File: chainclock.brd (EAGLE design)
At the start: 60 x 40 mm, 11 parts

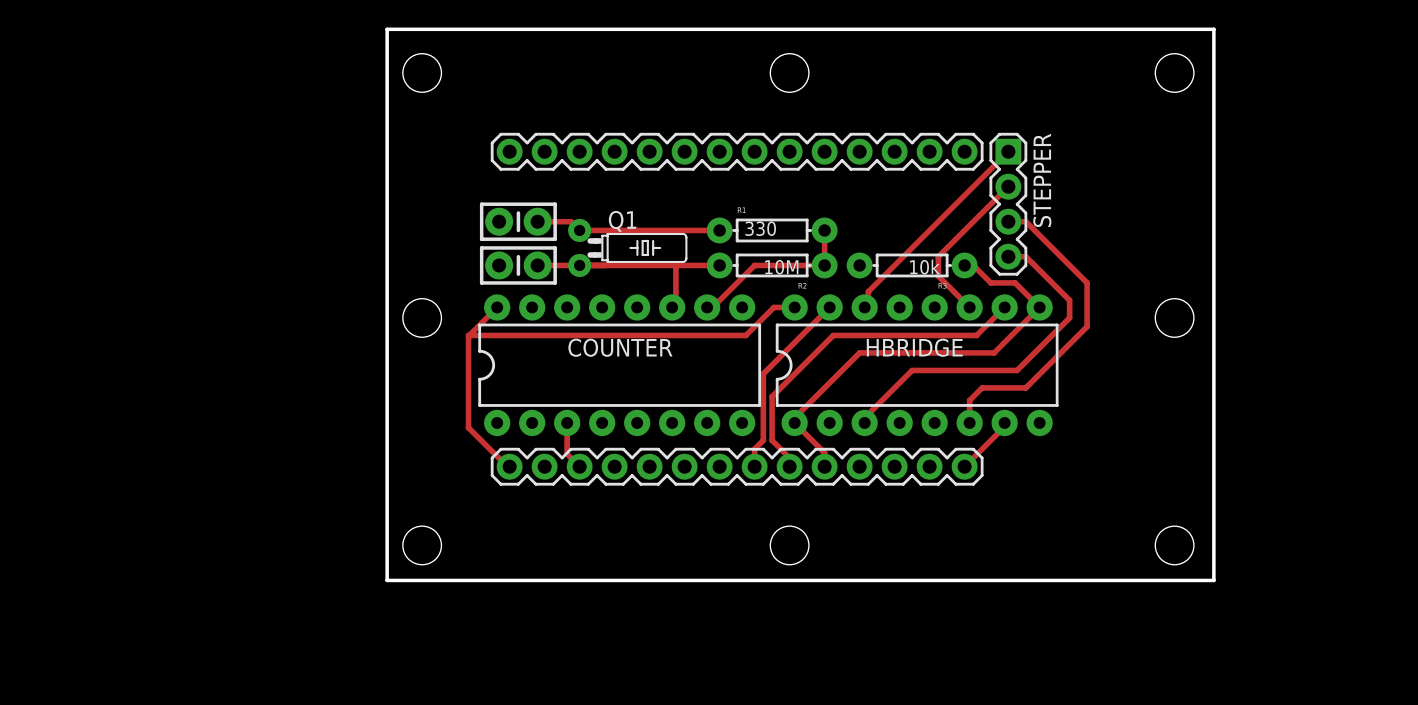
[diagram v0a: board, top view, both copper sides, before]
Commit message: Updates to chainclock, adding motor
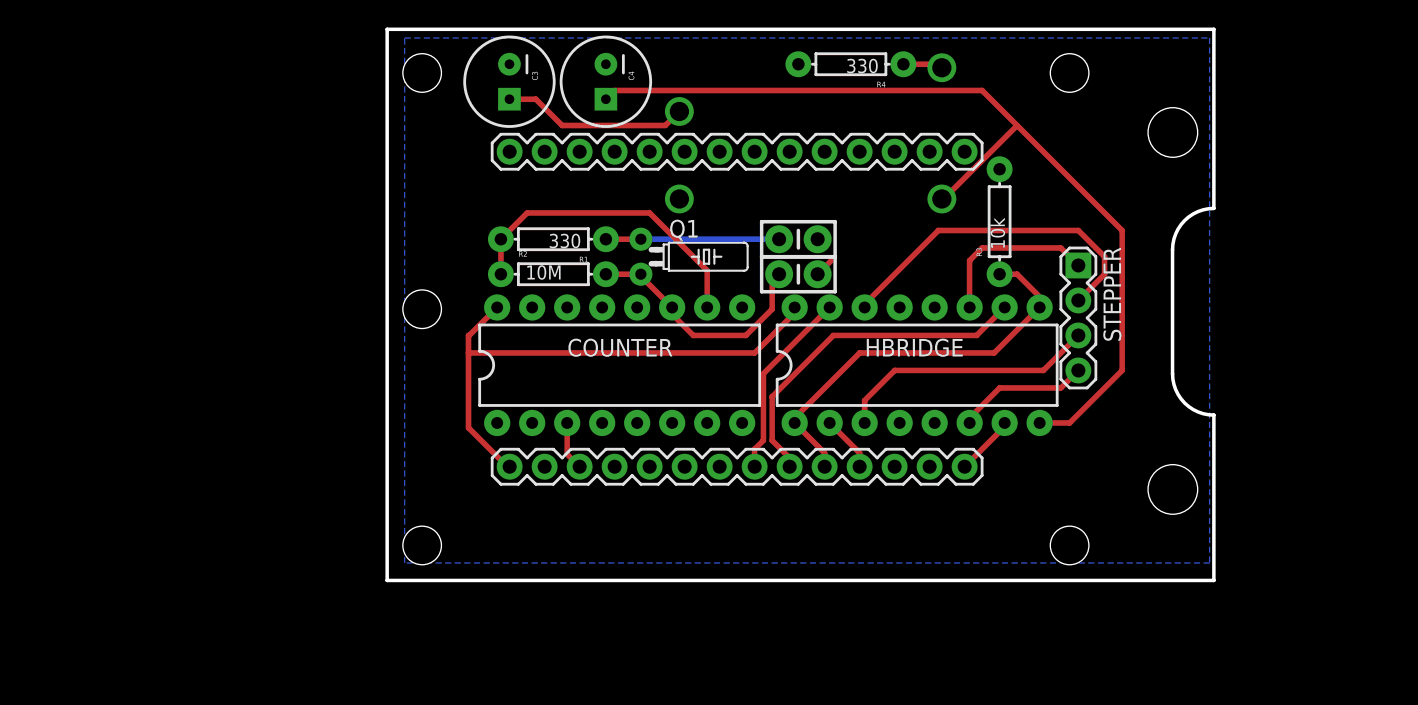
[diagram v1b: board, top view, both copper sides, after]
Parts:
- added C3, C4: (no value), SparkFun-Passives:CPOL-RADIAL-100UF-25V
- added R4: 330, SparkFun-Resistors:AXIAL-0.3EZ
- added U$1: PTN0405C, desjardins:EUU4
- added U$2: (no value), desjardins:NEMA14
- moved C2 20.4 mm to (29.8, 24.8), turned to 0 degrees
- moved C1 20.3 mm to (29.8, 22.2), turned to 0 degrees
- moved R1 15.9 mm to (12.1, 24.8), turned to 180 degrees
- moved R2 15.9 mm to (12.1, 22.2), turned to 0 degrees
- moved STEPPER 9.69 mm to (50.2, 22.9)
- moved R3 7.10 mm to (44.5, 26.0), turned to 90 degrees
- moved Q1 4.49 mm to (18.4, 23.5)
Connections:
- new net N$3: R4.P$1, U$1.3
- new net VDD12: C4.1, HBRIDGE.8, U$1.4
- new net VIN: C3.1, U$1.2
- net 1A: now also ARDUNOFIO.11
- net 1Y: now also STEPPER.3; no longer STEPPER.4
- net 2Y: now also STEPPER.4; no longer STEPPER.3
- net 3Y: now also STEPPER.1; no longer STEPPER.2
- net 4Y: now also STEPPER.2; no longer STEPPER.1
- net GND: now also C3.2, C4.2, R4.P$2, U$1.1
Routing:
- net VDD12: track 0.00 -> 67.3 mm
- net VIN: track 0.00 -> 13.5 mm
- net 2Y: track 23.1 -> 9.68 mm
- net RTC: track 12.3 -> 22.7 mm
- net 4Y: track 15.6 -> 24.6 mm
- net 1Y: track 25.3 -> 19.1 mm
- net 1A: track 0.00 -> 4.08 mm
- net N$3: track 0.00 -> 2.90 mm
- net EN: track 32.2 -> 30.1 mm
- net GND: track 0.00 -> 1.36 mm
- net N$1: track 13.5 -> 12.6 mm
- net 3V32: track 38.2 -> 39.0 mm
- added copper zone on layer 16, net GND
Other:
- outline, holes or cut-outs redrawn

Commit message: Move some stuff around
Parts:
- removed FRAME1: FRAME-LETTER, SparkFun-Aesthetics:CREATIVE_COMMONS
- R4: value 330 -> 1.35k
- moved C4 24.8 mm to (40.6, 36.2)
- moved STEPPER 10.3 mm to (42.5, 29.8)
- moved R4 5.08 mm to (28.6, 37.5)
- moved U$1 5.08 mm to (14.6, 38.7)
- moved ARDUNOFIO 4.45 mm to (38.7, 6.99)
- moved C1 4.45 mm to (25.4, 22.2)
- moved C2 4.45 mm to (25.4, 24.8)
- moved COUNTER 4.45 mm to (12.4, 15.6)
- moved HBRIDGE 4.45 mm to (34.0, 15.6)
- moved R3 4.45 mm to (40.0, 26.0)
- moved R1 4.44 mm to (7.62, 24.8)
- moved R2 4.44 mm to (7.62, 22.2)
- moved Q1 4.44 mm to (14.0, 23.5)
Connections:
- net 1Y: now also STEPPER.4; no longer STEPPER.3
- net 2Y: now also STEPPER.3; no longer STEPPER.4
- net 3Y: now also STEPPER.2; no longer STEPPER.1
- net 4Y: now also STEPPER.1; no longer STEPPER.2
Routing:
- net VDD12: track 67.3 -> 36.7 mm
- net 2Y: track 9.68 -> 18.1 mm
- net 4Y: track 24.6 -> 16.6 mm
- net VIN: track 13.5 -> 7.62 mm
- net 1Y: track 19.1 -> 22.3 mm
- net 3Y: track 12.2 -> 9.45 mm
- net EN: track 30.1 -> 29.6 mm

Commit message: Add logo
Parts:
- added U$3: (no value), desjardins:LOGO
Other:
- board text added: "cjd@chrisd.info http://blog.chrisd.info v1.0 (c) 2014"
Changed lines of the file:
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@@
 <wire x1="57" y1="24" x2="60" y2="27" width="0.254" layer="20" curve="-90"/>
 <wire x1="60" y1="27" x2="60" y2="40" width="0.254" layer="20"/>
+<text x="29.845" y="2.54" size="1.016" layer="21">cjd@chrisd.info
+http://blog.chrisd.info
+v1.0 (c) 2014</text>
 </plain>
 <attributes>
@@
 <element name="R4" library="SparkFun-Resistors" package="AXIAL-0.3EZ" value="1.35k" x="28.575" y="37.465" rot="R180"/>
 <element name="U$2" library="desjardins" package="NEMA14" value="" x="87.63" y="1.905" rot="R90"/>
+<element name="U$3" library="desjardins" package="LOGO" value="" x="5.08" y="1.905"/>
 </elements>
 <signals>
@@
 </board>
 </drawing>
+<compatibility>
+<note version="6.3" minversion="6.2.2" severity="warning">
+Since Version 6.2.2 text objects can contain more than one line,
+which will not be processed correctly with this version.
+</note>
+</compatibility>
 </eagle>

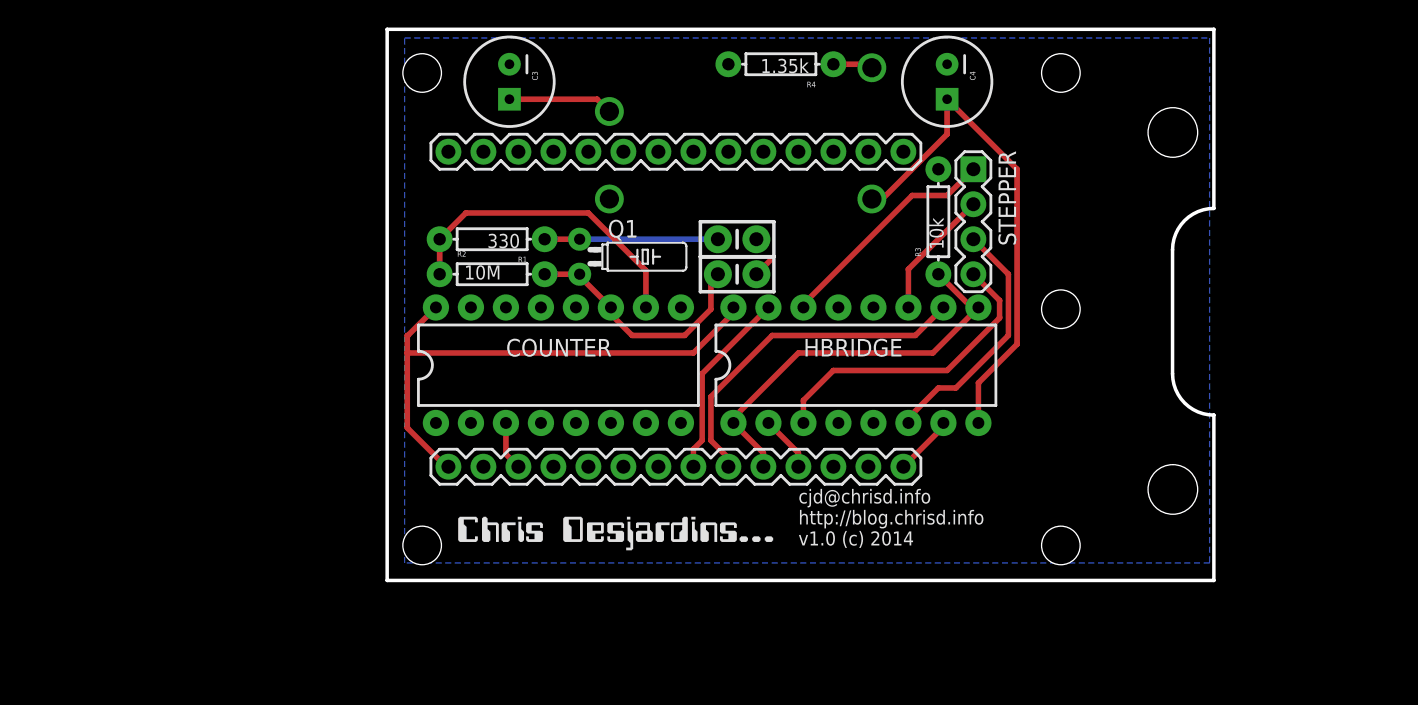
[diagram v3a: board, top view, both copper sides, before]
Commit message: Move around voltage reg
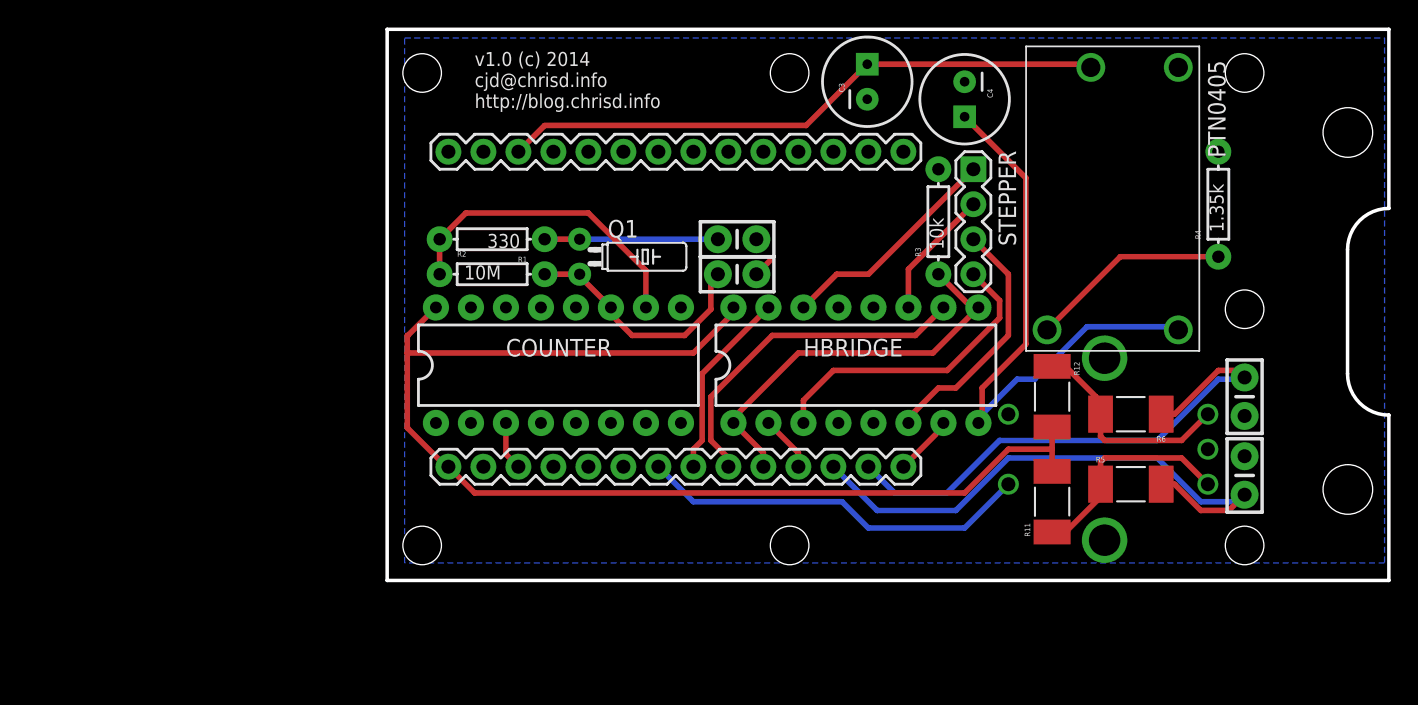
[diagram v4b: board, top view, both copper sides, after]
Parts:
- removed U$1: PTN0405C, desjardins:EUU4
- added C5, C6: .01uf, SparkFun-Capacitors:CAP-PTH-SMALL-KIT
- added PTN0405: PTN0405C, desjardins:EUU4
- added R11, R12, R5, R6: 10k, SparkFun-Resistors:R2010
- added SW1: ROTARTY_ENCODER, SparkFun-Electromechanical:ROTARY_ENC_PLAIN
- moved U$3 68.8 mm to (67.9, 29.8), flipped to the bottom, turned to 270 degrees
- moved R4 33.3 mm to (60.3, 27.3), turned to 90 degrees
- moved C3 26.0 mm to (34.8, 36.2), turned to 90 degrees
- moved U$2 12.7 mm to (100.3, 1.91)
- moved C4 1.80 mm to (41.9, 34.9)
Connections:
- removed net VIN: C3.1, U$1.2
- new net N$2: R11.1, R5.1, SW1.B
- new net N$5: R12.1, R6.2, SW1.A
- new net RENBTN: ARDUNOFIO.7, SW1.SW+
- new net RENCA: ARDUNOFIO.13, C5.1, R6.1
- new net RENCB: ARDUNOFIO.12, C6.1, R5.2
- net 3V31: now also C3.1, PTN0405.2
- net 3V32: now also R11.2, R12.2
- net GND: now also C5.2, C6.2, PTN0405.1, SW1.C, SW1.SW-; no longer U$1.1
- net N$3: now also PTN0405.3; no longer U$1.3
- net VDD12: now also PTN0405.4; no longer U$1.4
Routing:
- net 3V32: track 39.0 -> 88.2 mm
- net 3V31: track 0.00 -> 44.3 mm
- net RENCB: track 0.00 -> 41.6 mm
- net RENCA: track 0.00 -> 39.1 mm
- net RENBTN: track 0.00 -> 28.6 mm
- net N$2: track 0.00 -> 16.1 mm
- net N$5: track 0.00 -> 15.8 mm
- net N$3: track 2.90 -> 14.6 mm
- net VIN: track 7.62 -> 0.00 mm
- net VDD12: track 36.7 -> 43.2 mm
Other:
- board size 60 x 40 mm -> 72.7 x 40 mm
- board text added: "v1.0 (c) 2014 cjd@chrisd.info http://blog.chrisd.info"
- board text removed: "cjd@chrisd.info http://blog.chrisd.info v1.0 (c) 2014"

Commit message: Switch out crystal
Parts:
- removed C1, C2: 33pf, SparkFun-Capacitors:CAP-PTH-SMALL-KIT
- removed Q1: (no value), adafruit:TC26H
- removed R1: 330, SparkFun-Resistors:AXIAL-0.3EZ
- removed R2: 10M, SparkFun-Resistors:AXIAL-0.3EZ
- added U$4: SG30XXJC, desjardins:SG3030JC
- moved C4 5.24 mm to (36.8, 36.2)
- moved C3 4.92 mm to (29.9, 36.2), turned to 270 degrees
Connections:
- removed net N$1: C2.1, Q1.1, R1.P$1
- removed net RS: C1.1, COUNTER.11, Q1.2, R2.P$2
- net 3V32: now also U$4.1, U$4.4
- net GND: now also U$4.2; no longer C1.2, C2.2
- net RTC: now also U$4.3; no longer R1.P$2, R2.P$1
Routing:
- net RTC: track 22.7 -> 3.07 mm
- net RS: track 17.8 -> 0.00 mm
- net N$1: track 12.6 -> 0.00 mm
- net 3V32: track 88.2 -> 93.5 mm
- net GND: track 1.36 -> 2.78 mm
- net 3V31: track 44.3 -> 45.7 mm

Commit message: rework layout
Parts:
- moved U$4 63.1 mm to (26.0, 28.6), turned to 180 degrees
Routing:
- net GND: track 2.78 -> 9.65 mm
- net 3V32: track 93.5 -> 98.5 mm
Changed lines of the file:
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@@
 <element name="R5" library="SparkFun-Resistors" package="R2010" value="10k" x="53.975" y="6.985"/>
 <element name="R6" library="SparkFun-Resistors" package="R2010" value="10k" x="53.975" y="12.065" rot="R180"/>
-<element name="U$4" library="desjardins" package="SG3030JC" value="SG30XXJC" x="-26.035" y="-6.985"/>
+<element name="U$4" library="desjardins" package="SG3030JC" value="SG30XXJC" x="26.035" y="28.575" rot="R180"/>
 </elements>
 <signals>
@@
 <contactref element="C5" pad="2"/>
 <contactref element="SW1" pad="SW-"/>
-<wire x1="13.7" y1="19.812" x2="13.7" y2="22.59" width="0.4064" layer="1"/>
 <contactref element="U$4" pad="2"/>
 <contactref element="U$4" pad="2"/>
-<wire x1="6.985" y1="8.255" x2="-18.245" y2="-5.985" width="0" layer="19" extent="1-1"/>
+<wire x1="13.7" y1="19.812" x2="13.7" y2="23.03" width="0.4064" layer="1"/>
+<wire x1="13.7" y1="23.03" x2="18.245" y2="27.575" width="0.4064" layer="1"/>
 </signal>
 <signal name="3V30">
@@
 <wire x1="4.445" y1="8.255" x2="4.285" y2="8.255" width="0.4064" layer="1"/>
 <wire x1="4.285" y1="8.255" x2="1.46" y2="11.08" width="0.4064" layer="1"/>
-<wire x1="25.13" y1="19.812" x2="25.13" y2="19.415" width="0.4064" layer="1"/>
 <wire x1="25.13" y1="19.415" x2="22.225" y2="16.51" width="0.4064" layer="1"/>
 <wire x1="22.225" y1="16.51" x2="1.46" y2="16.51" width="0.4064" layer="1"/>
@@
 <wire x1="48.26" y1="9.525" x2="48.26" y2="11.135" width="0.4064" layer="1"/>
 <wire x1="48.26" y1="9.525" x2="48.26" y2="7.915" width="0.4064" layer="1"/>
-<wire x1="25.13" y1="19.812" x2="25.13" y2="22.86" width="0.4064" layer="1"/>
-<wire x1="25.13" y1="22.86" x2="25.13" y2="24.94" width="0.4064" layer="1"/>
-<wire x1="25.01" y1="22.74" x2="25.13" y2="22.86" width="0.4064" layer="1"/>
 <contactref element="U$4" pad="4"/>
 <contactref element="U$4" pad="1"/>
-<wire x1="-23.325" y1="-1.385" x2="-23.325" y2="-5.985" width="0" layer="19" extent="1-1"/>
-<wire x1="1.46" y1="11.08" x2="-23.325" y2="-1.385" width="0" layer="19" extent="1-1"/>
+<wire x1="25.13" y1="19.812" x2="25.13" y2="22.86" width="0.4064" layer="1"/>
+<wire x1="25.13" y1="22.86" x2="25.13" y2="25.77" width="0.4064" layer="1"/>
+<wire x1="25.13" y1="25.77" x2="23.325" y2="27.575" width="0.4064" layer="1"/>
+<wire x1="23.325" y1="22.975" x2="25.015" y2="22.975" width="0.4064" layer="1"/>
+<wire x1="25.015" y1="22.975" x2="25.13" y2="22.86" width="0.4064" layer="1"/>
+<wire x1="25.13" y1="19.415" x2="25.13" y2="19.812" width="0.4064" layer="1"/>
 </signal>
 <signal name="VDD12">
@@
 <signal name="RTC">
 <contactref element="COUNTER" pad="10"/>
-<wire x1="18.78" y1="19.812" x2="18.78" y2="19.955" width="0.4064" layer="1"/>
-<wire x1="18.78" y1="19.955" x2="17.78" y2="20.955" width="0.4064" layer="1"/>
-<wire x1="17.78" y1="20.955" x2="17.78" y2="22.47" width="0.4064" layer="1"/>
 <contactref element="U$4" pad="3"/>
-<wire x1="-18.245" y1="-1.385" x2="17.78" y2="20.955" width="0" layer="19" extent="1-1"/>
+<wire x1="18.245" y1="22.975" x2="18.245" y2="20.347" width="0.4064" layer="1"/>
+<wire x1="18.245" y1="20.347" x2="18.78" y2="19.812" width="0.4064" layer="1"/>
 </signal>
 </signals>

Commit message: Small updates
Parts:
- moved C6 1.91 mm to (62.2, 5.71)
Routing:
- net RENCB: track 41.6 -> 42.2 mm
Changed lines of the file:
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@@
 <plain>
 <hole x="2.54" y="2.54" drill="2.8"/>
-<hole x="2.54" y="36.83" drill="2.8"/>
+<hole x="2.54" y="37.465" drill="2.8"/>
 <wire x1="0" y1="0" x2="0" y2="40" width="0.254" layer="20"/>
 <wire x1="0" y1="40" x2="72.7" y2="40" width="0.254" layer="20"/>
@@
 http://blog.chrisd.info</text>
 <hole x="43.18" y="2.54" drill="2.8"/>
-<hole x="43.18" y="36.83" drill="2.8"/>
+<hole x="43.18" y="37.465" drill="2.8"/>
 </plain>
 <attributes>
@@
 <element name="SW1" library="SparkFun-Electromechanical" package="ROTARY_ENC_PLAIN" value="ROTARTY_ENCODER" x="52.07" y="9.525" rot="MR180"/>
 <element name="C5" library="SparkFun-Capacitors" package="CAP-PTH-SMALL-KIT" value=".01uf" x="62.23" y="13.335" rot="R270"/>
-<element name="C6" library="SparkFun-Capacitors" package="CAP-PTH-SMALL-KIT" value=".01uf" x="62.23" y="7.62" rot="R90"/>
+<element name="C6" library="SparkFun-Capacitors" package="CAP-PTH-SMALL-KIT" value=".01uf" x="62.23" y="5.715" rot="R90"/>
 <element name="R11" library="SparkFun-Resistors" package="R2010" value="10k" x="48.26" y="5.715" rot="R90"/>
 <element name="R12" library="SparkFun-Resistors" package="R2010" value="10k" x="48.26" y="13.335" rot="R270"/>
@@
 <contactref element="C6" pad="1"/>
 <contactref element="R5" pad="2"/>
-<wire x1="55.88" y1="8.89" x2="59.055" y2="5.715" width="0.4064" layer="16"/>
-<wire x1="59.055" y1="5.715" x2="61.722" y2="5.715" width="0.4064" layer="16"/>
-<wire x1="61.722" y1="5.715" x2="62.23" y2="6.223" width="0.4064" layer="16"/>
-<wire x1="59.055" y1="5.08" x2="61.087" y2="5.08" width="0.4064" layer="1"/>
-<wire x1="61.087" y1="5.08" x2="62.23" y2="6.223" width="0.4064" layer="1"/>
+<wire x1="55.88" y1="8.89" x2="60.325" y2="4.445" width="0.4064" layer="16"/>
 <wire x1="56.175" y1="6.985" x2="57.15" y2="6.985" width="0.4064" layer="1"/>
-<wire x1="57.15" y1="6.985" x2="59.055" y2="5.08" width="0.4064" layer="1"/>
+<wire x1="57.15" y1="6.985" x2="60.325" y2="3.81" width="0.4064" layer="1"/>
 <wire x1="35.56" y1="5.08" x2="39.37" y2="5.08" width="0.4064" layer="16"/>
 <wire x1="39.37" y1="5.08" x2="42.545" y2="8.255" width="0.4064" layer="16"/>
 <wire x1="42.545" y1="8.255" x2="44.45" y2="8.255" width="0.4064" layer="16"/>
 <wire x1="44.45" y1="8.255" x2="45.085" y2="8.89" width="0.4064" layer="16"/>
+<wire x1="60.325" y1="4.445" x2="62.103" y2="4.445" width="0.4064" layer="16"/>
+<wire x1="62.103" y1="4.445" x2="62.23" y2="4.318" width="0.4064" layer="16"/>
+<wire x1="60.325" y1="3.81" x2="61.722" y2="3.81" width="0.4064" layer="1"/>
+<wire x1="61.722" y1="3.81" x2="62.23" y2="4.318" width="0.4064" layer="1"/>
 </signal>
 <signal name="RENCA">
